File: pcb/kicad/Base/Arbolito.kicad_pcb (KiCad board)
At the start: 2 copper layers, 73 x 66 mm, 60 parts, among them J1 Battery, J2 Conn_01x06_Female, P1 USB_C_Plug_USB2.0, Q1 S8050, Q2 S8050, Q3 S8050, SW1 SW_DP3T, SW2 SW_Push, SW3 SW_Push, SW4 SW_Push, U1 NCP115AMX120TCG, U2 CH340C, U3 AP63205WU, U4 ESP-12F, U5 SHTC1

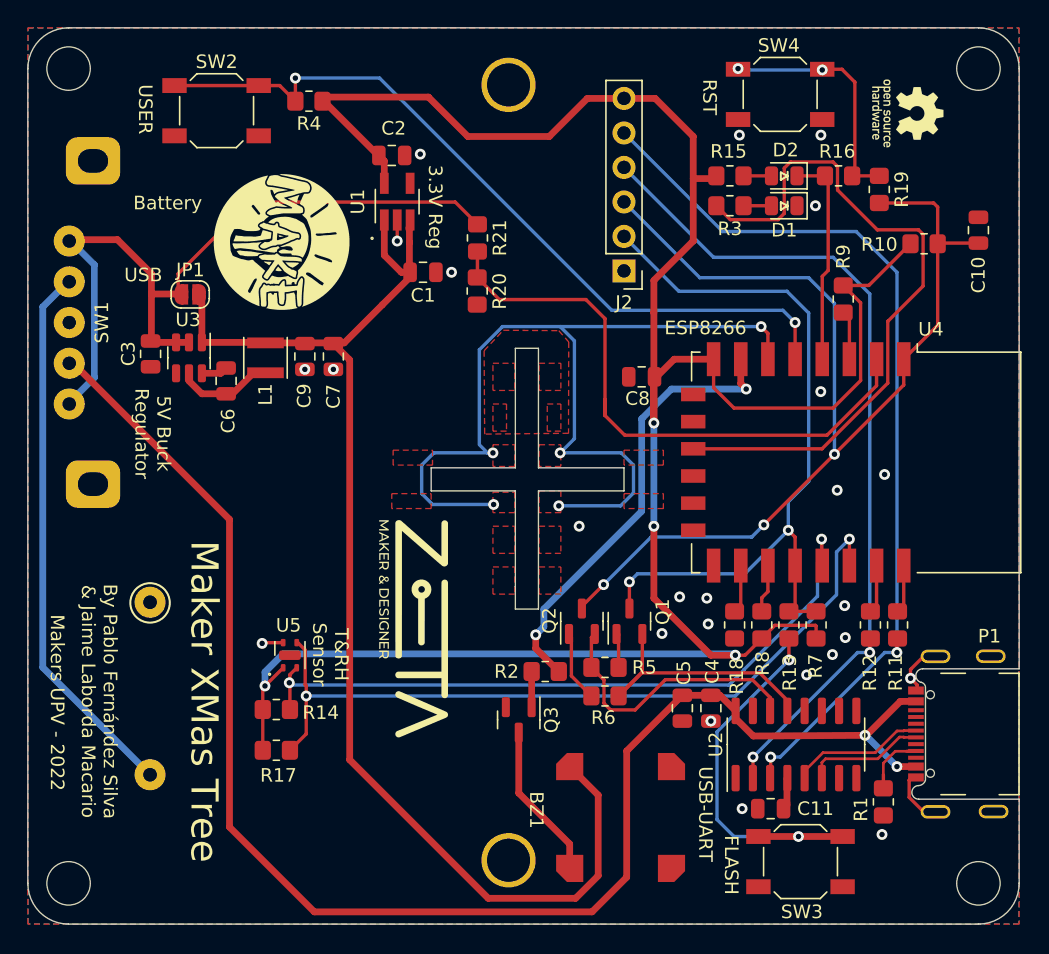
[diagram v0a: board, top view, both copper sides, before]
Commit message: SHT31 addition
SHT11 Temp sensor changed to SHT31.  Furthermore isolation slots where included
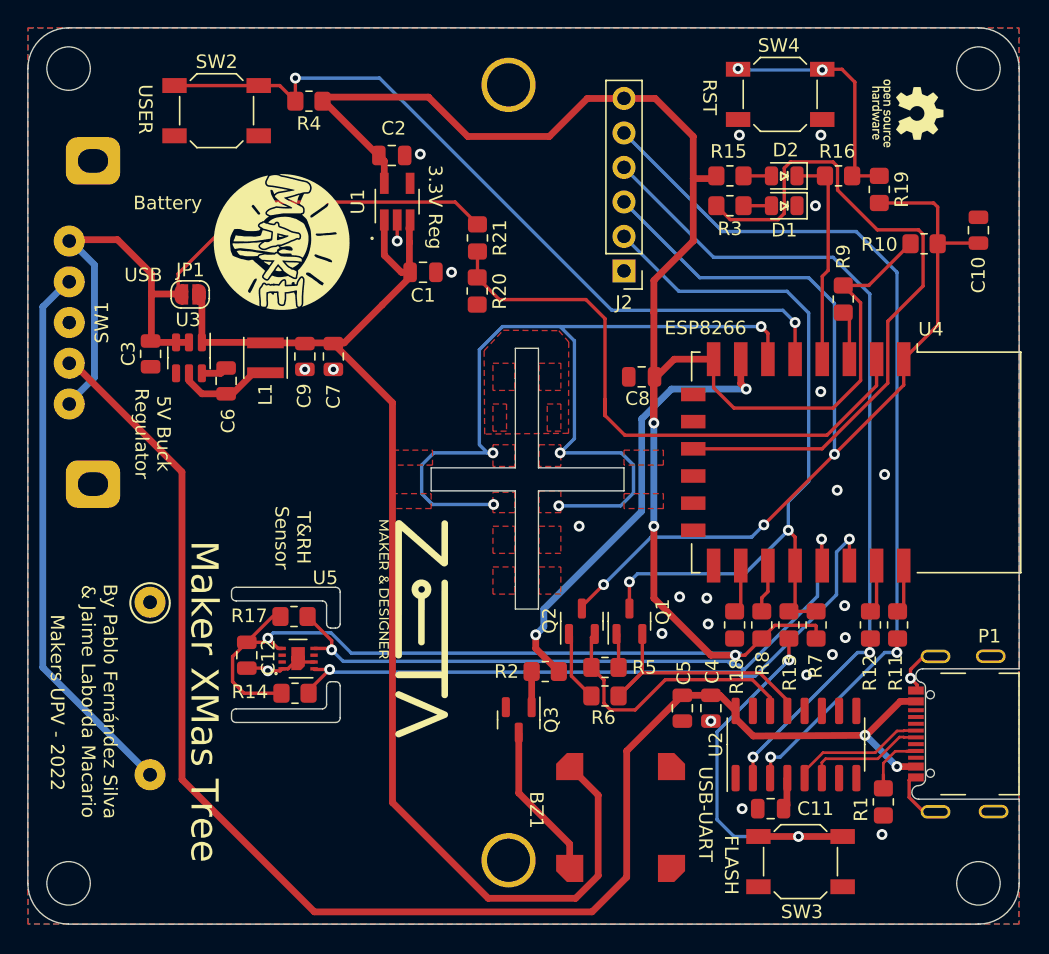
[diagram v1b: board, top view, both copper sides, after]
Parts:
- added C12: 0.1uF, Capacitor_SMD:C_0805_2012Metric, F.Cu at (121.1, 108.2)
- C8: value 100uF -> 10uF
- U5: value SHTC1 -> SHT31-DIS; footprint Sensor_Humidity:Sensirion_DFN-4-1EP_2x2mm_P1mm_EP0.7x1.6mm -> Sensor_Humidity:Sensirion_DFN-8-1EP_2.5x2.5mm_P0.5mm_EP1.1x1.7mm
- moved R17 9.94 mm to (124.6, 105.3)
- moved R14 1.83 mm to (124.7, 111.0)
- moved U5 0.65 mm to (124.9, 108.5), turned to 180 degrees
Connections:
- R14 pad 1: /SCL -> /SDA
- R17 pad 1: /SDA -> /SCL
- U5 pad 1: +3.3V -> /SDA
- U5 pad 2: /SCL -> GND
- U5 pad 3: /SDA -> unconnected-(U5-ALERT-Pad3)
- U5 pad 4: GND -> /SCL
- U5 pad 5: unconnected-(U5-NC-Pad5) -> +3.3V
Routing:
- net /SDA: track 57.5 -> 50.6 mm
- net +3.3V: track 170.5 -> 176.3 mm
- net GND: track 9.68 -> 13.6 mm
- net /SCL: track 51.2 -> 49.9 mm
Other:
- outline, holes or cut-outs redrawn

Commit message: Switch and buttons
Switch and buttons changed on PCB
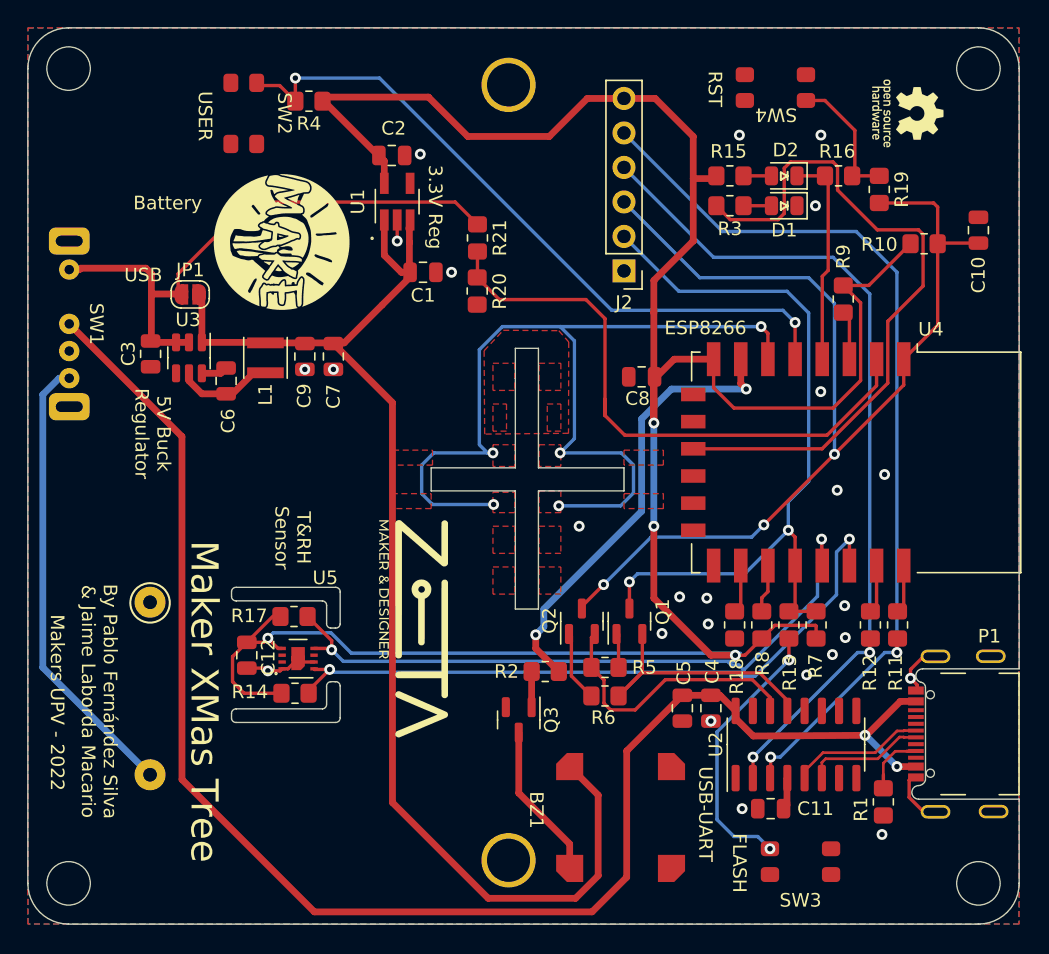
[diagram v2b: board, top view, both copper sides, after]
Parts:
- SW1: footprint Library:3PSwitch -> Library:3PSwitch_Cheap
- SW2, SW3, SW4: footprint Button_Switch_SMD:SW_SPST_SKQG_WithoutStem -> Library:Button
- moved SW1 3.50 mm to (106.3, 83.8), turned to -90 degrees
- moved SW2 2.01 mm to (120.9, 68.3), turned to -90 degrees
- moved SW4 0.61 mm to (160.1, 66.4), turned to 180 degrees
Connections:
- SW1 pad 1: VBUS -> VCC
- SW1 pad 2: unconnected-(SW1-Pad2) -> VBUS
- SW1 pad 3: VCC -> unconnected-(SW1-Pad3)
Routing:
- net VCC: track 57.2 -> 42.9 mm
- net Net-(R16-Pad1): track 18.1 -> 9.94 mm, vias 2 -> 0
- net Net-(R13-Pad1): track 28.4 -> 20.5 mm
- net Net-(J1-Pin_2): track 40.5 -> 33.7 mm
- net /Boton: track 58.1 -> 51.9 mm
- net VBUS: track 111.9 -> 114.6 mm
